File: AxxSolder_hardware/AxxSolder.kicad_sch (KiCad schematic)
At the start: 141 parts, among them IC1 TLV76733DRVR, IC2 OPA2387DSGT, IC3 LMR54406DBVR, IC4 STM32G431CBT6, IC5 TPD4E1U06DBVR, IC6 STUSB4500QTR, IC7 MAX16171ATA_VY+T, IC8 LTC4440AHMS8E, J1 USB4110-GF-A, J2 691243110009, J3 TSW-102-07-T-S, J4 61300611821, J5 TSW-102-07-T-S, J6 TSW-102-07-T-S, Q1 STL9P3LLH6, Q2 STL10N3LLH5, Q3 2N7002NXAKR, U2 PEC11J-9215F-S0015, U3 BSC014N04LS

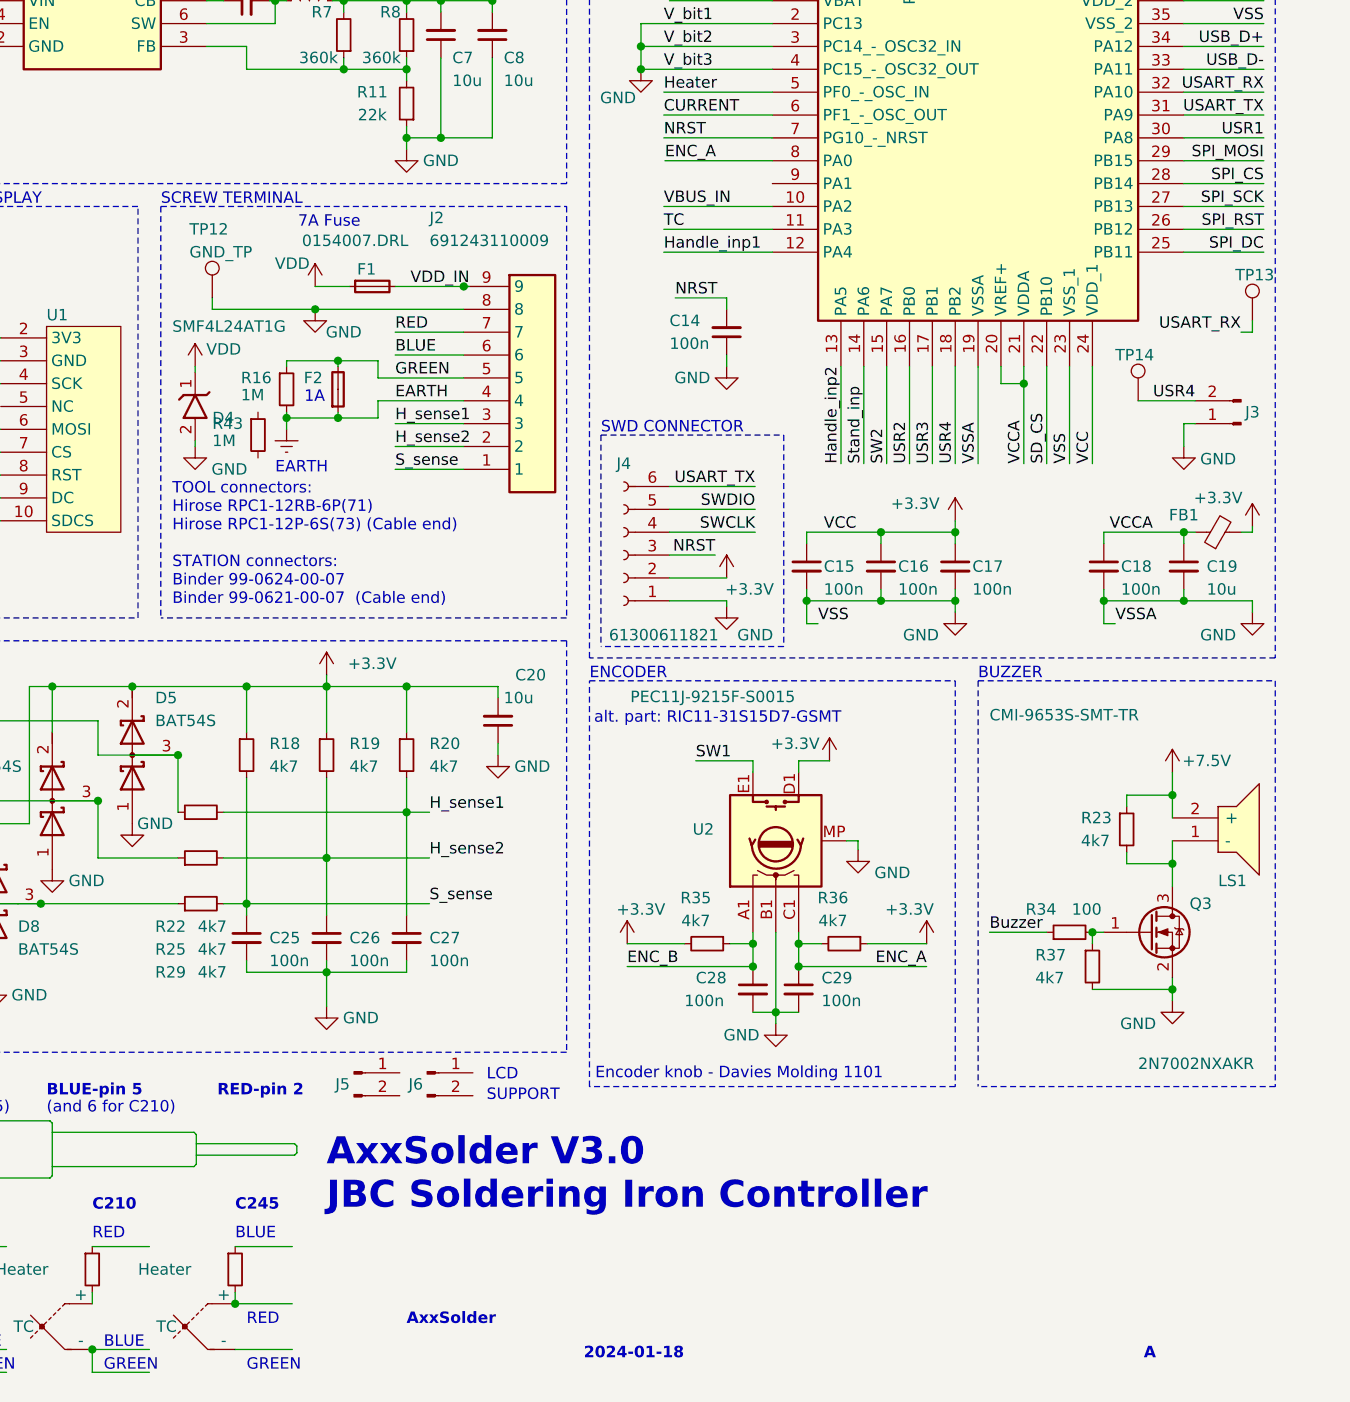
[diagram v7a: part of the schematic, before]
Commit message: update design with I_LEAK current sensor
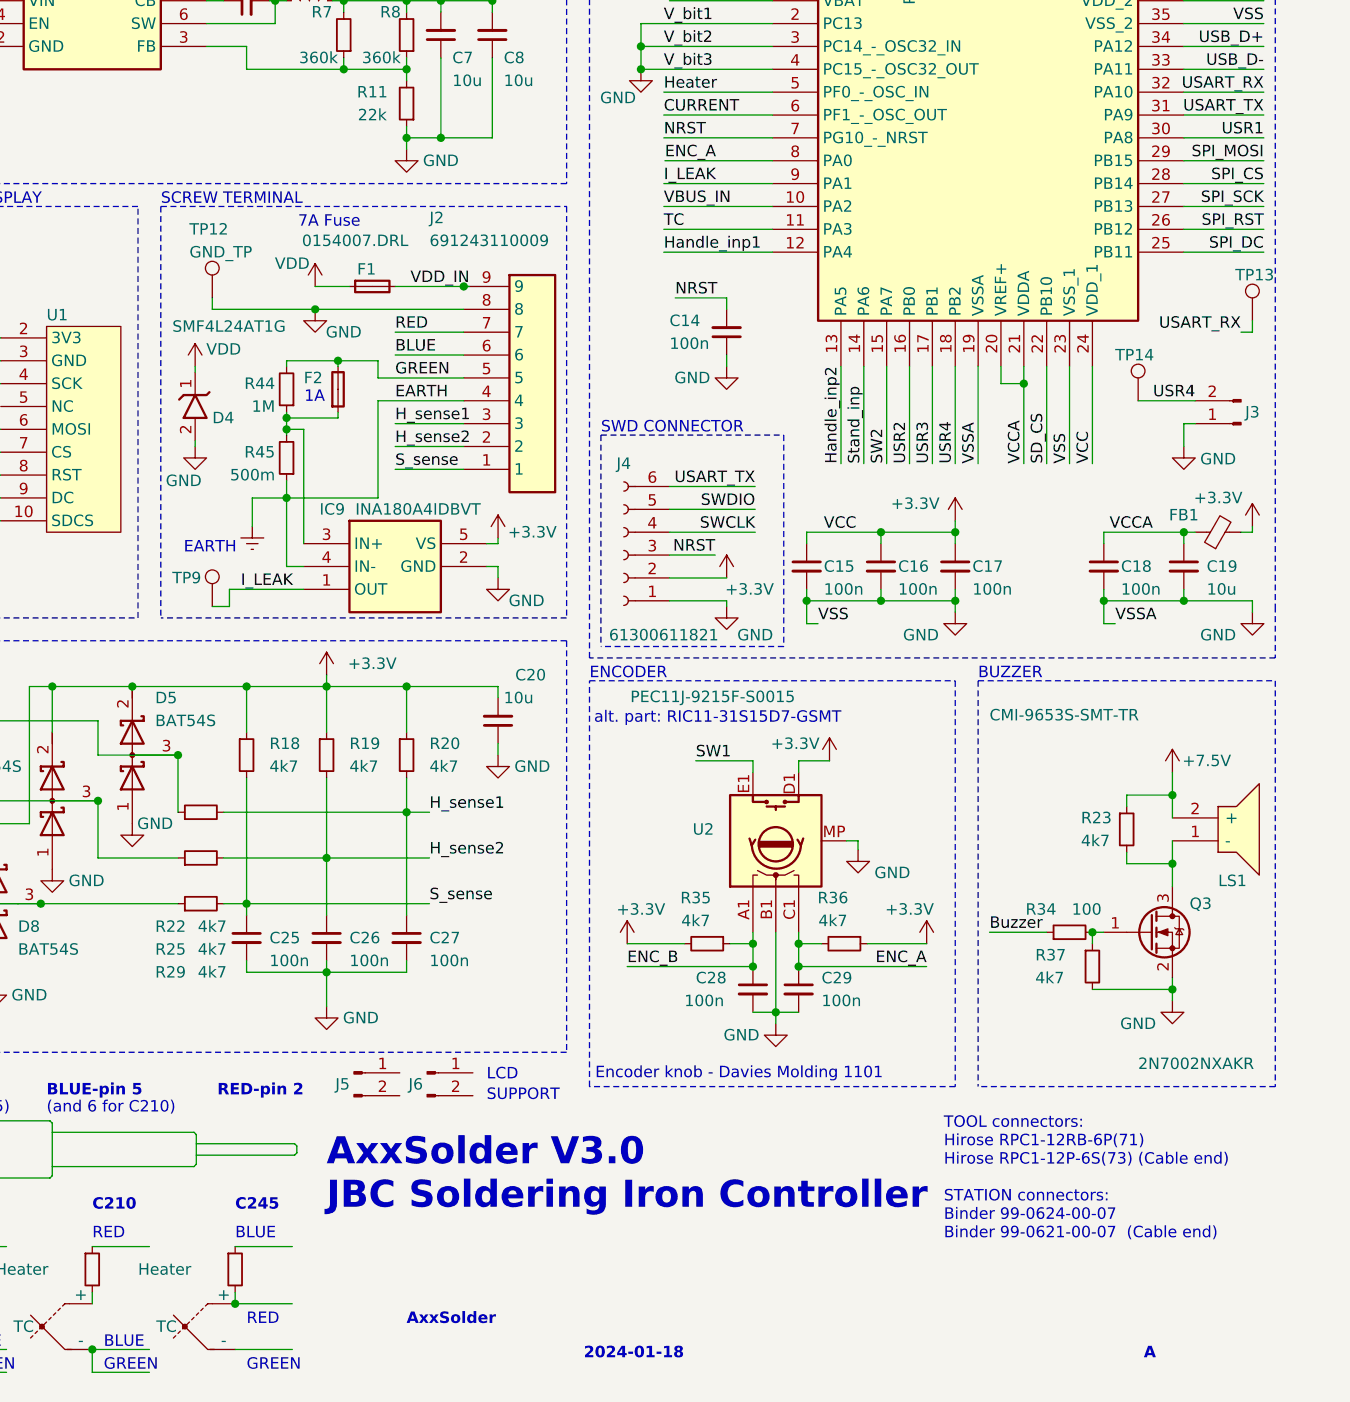
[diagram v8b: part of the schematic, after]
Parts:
- removed R16, R43: 1M, Resistor_SMD:R_1206_3216Metric, symbol Device:R_Small
- added IC9: INA180A4IDBVT, footprints:SOT95P280X145-5N, symbol INA180A4IDBVT:INA180A4IDBVT
- added R44: 1M, Resistor_SMD:R_0805_2012Metric, symbol Device:R_Small
- added R45: 500m, Resistor_SMD:R_0805_2012Metric, symbol Device:R_Small
- added TP9: Current_TP, TestPoint:TestPoint_Pad_D1.0mm, symbol Connector:TestPoint
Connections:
- net +3.3V: now also IC9.5 (VS)
- net Earth: now also IC9.4 (IN-), R45.1; no longer F2.1
- net GND: now also IC9.2 (GND)
- net GREEN: now also R44.2
- net I_LEAK: now reaches IC4.9 (PA1)
- net I_LEAK: now also IC9.1 (OUT), TP9.1
- new net: F2.1, IC9.3 (IN+), R44.1, R45.2
